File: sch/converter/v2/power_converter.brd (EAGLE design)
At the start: 54.6 x 28.2 mm, 23 parts

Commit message: Carrier board
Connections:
- new net SCL: U$1.P$29, U$1.P$30
- new net SDA: U$1.P$27, U$1.P$28
- net EXTVCC: no longer U$1.P$27, U$1.P$28, U$1.P$29, U$1.P$30
- net INTVCC: no longer U$1.P$23, U$1.P$24, U$1.P$25, U$1.P$26
- net PGOOD: now also U$1.P$25, U$1.P$26; no longer U$1.P$21, U$1.P$22
- net RUN: now also U$1.P$23, U$1.P$24; no longer U$1.P$19, U$1.P$20
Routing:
- net INTVCC: track 35.9 -> 0.00 mm, vias 3 -> 0
- net EXTVCC: track 31.0 -> 0.00 mm, vias 2 -> 0
- net SDA: track 0.00 -> 4.67 mm, vias 0 -> 1
- net SCL: track 0.00 -> 4.67 mm, vias 0 -> 1
- net PGOOD: track 12.5 -> 15.1 mm
- net RUN: track 18.7 -> 20.8 mm
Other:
- board text added: "ALAIN L. 10/2018"
- board text added: "REV: 2.1"
- board text added: "VIN: 4.5 to 36V"
- board text added: "VOUT: 0.8 to 24V"
- board text removed: "0.8 to 24V"
- board text removed: "4.5 to 36V"
- board text removed: "ALAIN L. 09/2018"
- board text removed: "REV: 2.0"

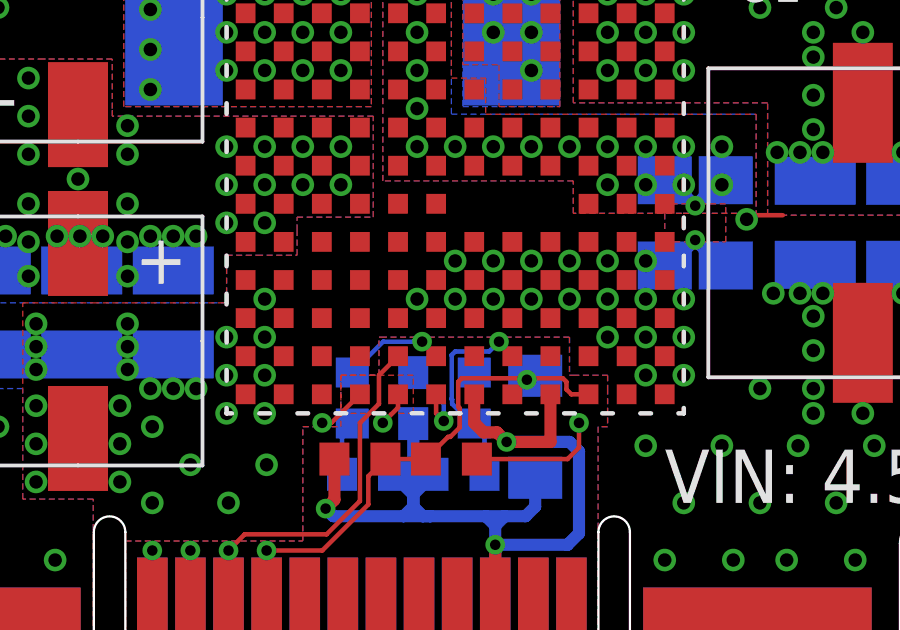
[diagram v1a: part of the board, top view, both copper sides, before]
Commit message: Added carrier BOM; Chaned carrier MOSFETs
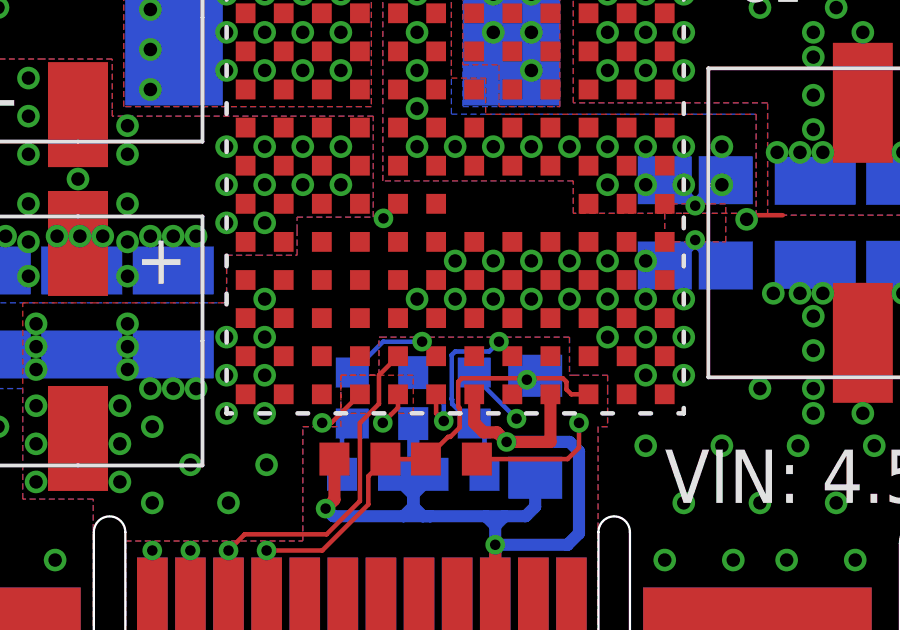
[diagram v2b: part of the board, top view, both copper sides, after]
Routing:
- net INTVCC: track 0.00 -> 18.4 mm, vias 0 -> 2
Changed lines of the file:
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@@
 <contactref element="U1" pad="F5"/>
 <contactref element="R6" pad="2"/>
-<wire x1="23.495" y1="27.2025" x2="20.955" y2="32.8295" width="0" layer="19" extent="1-16"/>
+<wire x1="20.955" y1="32.8295" x2="20.4696" y2="32.3441" width="0.1524" layer="1"/>
+<via x="20.4696" y="32.3441" extent="1-16" drill="0.35"/>
+<wire x1="20.4696" y1="32.3441" x2="20.4696" y2="31.5186" width="0.1524" layer="15"/>
+<wire x1="17.896" y1="25.7467875" x2="17.896" y2="25.3072125" width="0.1524" layer="15"/>
+<wire x1="18.7325" y1="26.5832875" x2="17.896" y2="25.7467875" width="0.1524" layer="15"/>
+<wire x1="17.896" y1="25.3072125" x2="18.2477125" y2="24.9555" width="0.1524" layer="15"/>
+<wire x1="18.7325" y1="29.7815" x2="18.7325" y2="26.5832875" width="0.1524" layer="15"/>
+<via x="24.90506875" y="25.66706875" extent="1-16" drill="0.35"/>
+<wire x1="24.3547125" y1="25.4226" x2="24.6606" y2="25.4226" width="0.1524" layer="15"/>
+<wire x1="24.6606" y1="25.4226" x2="24.90506875" y2="25.66706875" width="0.1524" layer="15"/>
+<wire x1="23.8876125" y1="24.9555" x2="24.3547125" y2="25.4226" width="0.1524" layer="15"/>
+<wire x1="18.2477125" y1="24.9555" x2="23.8876125" y2="24.9555" width="0.1524" layer="15"/>
+<wire x1="24.90506875" y1="25.66706875" x2="23.495" y2="27.0771375" width="0.1524" layer="16"/>
+<wire x1="23.495" y1="27.0771375" x2="23.495" y2="27.2025" width="0.1524" layer="16"/>
+<wire x1="20.4696" y1="31.5186" x2="18.7325" y2="29.7815" width="0.1524" layer="15"/>
 </signal>
 <signal name="PGOOD">

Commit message: Updated CAM files
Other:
- board text added: "NOTES: 1. Solder board in the folowing order: 1.1 Reflow solder top side using leaded solder paste with stencil 1.2 Hand solder bottom side 2. Solid silk-screen square to be used for noting designed output voltage 3. Card-edge style board fits into TE Connectivity Mini Crown Edge Connector P3S12 1926155-2"
- board text added: "REV: 2.0"
- board text removed: "Card-edge style board fits into TE Connectivity Mini Crown Edge Connector P3S12 1926155-2"
- board text removed: "REV: 2.1"
- board text removed: "Solid silk-screen square to be used for noting designed output voltage"
- board text removed: "Stencil and reflow soldering are required for board assembly"
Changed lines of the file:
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@@
 <?xml version="1.0" encoding="utf-8"?>
 <!DOCTYPE eagle SYSTEM "eagle.dtd">
-<eagle version="9.1.3">
+<eagle version="9.2.1">
 <drawing>
 <settings>
@@
 <grid distance="50" unitdist="mil" unit="mil" style="dots" multiple="1" display="yes" altdistance="2.5" altunitdist="mil" altunit="mil"/>
 <layers>
-<layer number="1" name="Top" color="4" fill="1" visible="yes" active="yes"/>
-<layer number="2" name="Route2" color="1" fill="3" visible="yes" active="yes"/>
+<layer number="1" name="Top" color="4" fill="1" visible="no" active="yes"/>
+<layer number="2" name="Route2" color="1" fill="3" visible="no" active="yes"/>
 <layer number="3" name="Route3" color="4" fill="3" visible="no" active="no"/>
 <layer number="4" name="Route4" color="1" fill="4" visible="no" active="no"/>
@@
 <layer number="13" name="Route13" color="4" fill="5" visible="no" active="no"/>
 <layer number="14" name="Route14" color="1" fill="6" visible="no" active="no"/>
-<layer number="15" name="Route15" color="4" fill="6" visible="yes" active="yes"/>
-<layer number="16" name="Bottom" color="1" fill="1" visible="yes" active="yes"/>
+<layer number="15" name="Route15" color="4" fill="6" visible="no" active="yes"/>
+<layer number="16" name="Bottom" color="1" fill="1" visible="no" active="yes"/>
 <layer number="17" name="Pads" color="2" fill="1" visible="yes" active="yes"/>
 <layer number="18" name="Vias" color="2" fill="1" visible="yes" active="yes"/>
-<layer number="19" name="Unrouted" color="6" fill="1" visible="yes" active="yes"/>
+<layer number="19" name="Unrouted" color="6" fill="1" visible="no" active="yes"/>
 <layer number="20" name="Dimension" color="24" fill="1" visible="yes" active="yes"/>
 <layer number="21" name="tPlace" color="7" fill="1" visible="yes" active="yes"/>
-<layer number="22" name="bPlace" color="7" fill="1" visible="yes" active="yes"/>
-<layer number="23" name="tOrigins" color="15" fill="1" visible="yes" active="yes"/>
-<layer number="24" name="bOrigins" color="15" fill="1" visible="yes" active="yes"/>
+<layer number="22" name="bPlace" color="7" fill="1" visible="no" active="yes"/>
+<layer number="23" name="tOrigins" color="15" fill="1" visible="no" active="yes"/>
+<layer number="24" name="bOrigins" color="15" fill="1" visible="no" active="yes"/>
 <layer number="25" name="tNames" color="7" fill="1" visible="yes" active="yes"/>
-<layer number="26" name="bNames" color="7" fill="1" visible="yes" active="yes"/>
+<layer number="26" name="bNames" color="7" fill="1" visible="no" active="yes"/>
 <layer number="27" name="tValues" color="7" fill="1" visible="no" active="yes"/>
 <layer number="28" name="bValues" color="7" fill="1" visible="no" active="yes"/>
 <layer number="29" name="tStop" color="7" fill="3" visible="yes" active="yes"/>
-<layer number="30" name="bStop" color="7" fill="6" visible="yes" active="yes"/>
+<layer number="30" name="bStop" color="7" fill="6" visible="no" active="yes"/>
 <layer number="31" name="tCream" color="7" fill="4" visible="yes" active="yes"/>
-<layer number="32" name="bCream" color="7" fill="5" visible="yes" active="yes"/>
-<layer number="33" name="tFinish" color="6" fill="3" visible="no" active="yes"/>
+<layer number="32" name="bCream" color="7" fill="5" visible="no" active="yes"/>
+<layer number="33" name="tFinish" color="6" fill="3" visible="yes" active="yes"/>
 <layer number="34" name="bFinish" color="6" fill="6" visible="no" active="yes"/>
 <layer number="35" name="tGlue" color="7" fill="4" visible="no" active="yes"/>
@@
 <layer number="37" name="tTest" color="7" fill="1" visible="no" active="yes"/>
 <layer number="38" name="bTest" color="7" fill="1" visible="no" active="yes"/>
-<layer number="39" name="tKeepout" color="4" fill="11" visible="yes" active="yes"/>
-<layer number="40" name="bKeepout" color="1" fill="11" visible="yes" active="yes"/>
-<layer number="41" name="tRestrict" color="4" fill="10" visible="yes" active="yes"/>
-<layer number="42" name="bRestrict" color="1" fill="10" visible="yes" active="yes"/>
+<layer number="39" name="tKeepout" color="4" fill="11" visible="no" active="yes"/>
+<layer number="40" name="bKeepout" color="1" fill="11" visible="no" active="yes"/>
+<layer number="41" name="tRestrict" color="4" fill="10" visible="no" active="yes"/>
+<layer number="42" name="bRestrict" color="1" fill="10" visible="no" active="yes"/>
 <layer number="43" name="vRestrict" color="2" fill="10" visible="no" active="yes"/>
 <layer number="44" name="Drills" color="7" fill="1" visible="no" active="yes"/>
 <layer number="45" name="Holes" color="7" fill="1" visible="no" active="yes"/>
-<layer number="46" name="Milling" color="3" fill="1" visible="yes" active="yes"/>
+<layer number="46" name="Milling" color="3" fill="1" visible="no" active="yes"/>
 <layer number="47" name="Measures" color="7" fill="1" visible="yes" active="yes"/>
 <layer number="48" name="Document" color="7" fill="1" visible="yes" active="yes"/>
@@
 <text x="40.7035" y="41.9735" size="1.27" layer="22" rot="MR180" align="bottom-right">MAX: 5A(Boost)
 10A(Buck)</text>
-<text x="83.82" y="10.16" size="1.778" layer="49">Stencil and reflow soldering
-are required for board assembly</text>
-<text x="83.82" y="0" size="1.778" layer="49">Solid silk-screen square to be used
-for noting designed output voltage</text>
-<text x="83.82" y="-13.97" size="1.778" layer="49">Card-edge style board fits into
-TE Connectivity Mini Crown Edge
-Connector P3S12 1926155-2</text>
+<text x="-96.52" y="-53.34" size="1.778" layer="49">NOTES:
+1. Solder board in the folowing order:
+  1.1 Reflow solder top side using leaded solder paste with stencil
+  1.2 Hand solder bottom side
+2. Solid silk-screen square to be used for noting designed output voltage
+3. Card-edge style board fits into TE Connectivity Mini Crown Edge Connector P3S12 1926155-2</text>
 <text x="2.54" y="43.1165" size="1.27" layer="21" align="top-center">REV:
-2.1</text>
+2.0</text>
 <dimension x1="62.23" y1="16.51" x2="62.23" y2="44.45" x3="71.12" y3="30.48" textsize="1.778" layer="48" visible="yes"/>
 <rectangle x1="43.18" y1="34.29" x2="50.8" y2="41.91" layer="25"/>
@@
 <attribute name="VALUE" x="19.05" y="22.4155" size="1.27" layer="27"/>
 </element>
-<element name="U$5" library="frames" library_urn="urn:adsk.eagle:library:229" package="A4L-LOC" value="" x="-104.14" y="-60.96"/>
-<element name="C7" library="LTM4607" package="PCR1H181MCL1GS" value="180u" x="36.449" y="32.1945"/>
+<element name="U$5" library="frames" library_urn="urn:adsk.eagle:library:229" package="A4L-LOC" value="" x="-104.14" y="-60.96" smashed="yes">
+<attribute name="DRAWING_NAME" x="113.03" y="-45.72" size="2.54" layer="48" font="vector"/>
+<attribute name="LAST_DATE_TIME" x="113.03" y="-50.8" size="2.286" layer="48" font="vector"/>
+</element>
+<element name="C7" library="LTM4607" package="PCR1H181MCL1GS" value="180u" x="36.449" y="32.1945" smashed="yes"/>
 <element name="R8" library="rcl" library_urn="urn:adsk.eagle:library:334" package="R0603" package3d_urn="urn:adsk.eagle:package:23555/2" value="6.98k" x="19.939" y="23.8125" smashed="yes" rot="MR0">
 <attribute name="SPICEPREFIX" value="R" x="19.939" y="23.8125" size="1.778" layer="28" rot="MR0" display="off"/>
@@
 </element>
 <element name="C14" library="LTM4607" package="PCR1V221MCL1GS" value="220u" x="10.287" y="39.0525" smashed="yes" rot="R180"/>
-<element name="U$1" library="LTM4607" package="1926155-2_CARD" value="1926155-2_CARD" x="25.4" y="16.51"/>
+<element name="U$1" library="LTM4607" package="1926155-2_CARD" value="1926155-2_CARD" x="25.4" y="16.51" smashed="yes"/>
 <element name="C2" library="rcl" library_urn="urn:adsk.eagle:library:334" package="C1210" package3d_urn="urn:adsk.eagle:package:23619/2" value="10u" x="7.366" y="29.21" smashed="yes" rot="MR270">
 <attribute name="SPICEPREFIX" value="C" x="7.366" y="29.21" size="1.778" layer="28" rot="MR270" display="off"/>

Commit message: Carrier rev. 1.4
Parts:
- added U$2: (no value), oshw:OSHW_8MM
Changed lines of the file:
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@@
 <?xml version="1.0" encoding="utf-8"?>
 <!DOCTYPE eagle SYSTEM "eagle.dtd">
-<eagle version="9.2.1">
+<eagle version="9.4.2">
 <drawing>
 <settings>
@@
 <grid distance="50" unitdist="mil" unit="mil" style="dots" multiple="1" display="yes" altdistance="2.5" altunitdist="mil" altunit="mil"/>
 <layers>
-<layer number="1" name="Top" color="4" fill="1" visible="no" active="yes"/>
-<layer number="2" name="Route2" color="1" fill="3" visible="no" active="yes"/>
+<layer number="1" name="Top" color="4" fill="1" visible="yes" active="yes"/>
+<layer number="2" name="Route2" color="1" fill="3" visible="yes" active="yes"/>
 <layer number="3" name="Route3" color="4" fill="3" visible="no" active="no"/>
 <layer number="4" name="Route4" color="1" fill="4" visible="no" active="no"/>
@@
 <layer number="13" name="Route13" color="4" fill="5" visible="no" active="no"/>
 <layer number="14" name="Route14" color="1" fill="6" visible="no" active="no"/>
-<layer number="15" name="Route15" color="4" fill="6" visible="no" active="yes"/>
-<layer number="16" name="Bottom" color="1" fill="1" visible="no" active="yes"/>
+<layer number="15" name="Route15" color="4" fill="6" visible="yes" active="yes"/>
+<layer number="16" name="Bottom" color="1" fill="1" visible="yes" active="yes"/>
 <layer number="17" name="Pads" color="2" fill="1" visible="yes" active="yes"/>
 <layer number="18" name="Vias" color="2" fill="1" visible="yes" active="yes"/>
-<layer number="19" name="Unrouted" color="6" fill="1" visible="no" active="yes"/>
+<layer number="19" name="Unrouted" color="6" fill="1" visible="yes" active="yes"/>
 <layer number="20" name="Dimension" color="24" fill="1" visible="yes" active="yes"/>
 <layer number="21" name="tPlace" color="7" fill="1" visible="yes" active="yes"/>
-<layer number="22" name="bPlace" color="7" fill="1" visible="no" active="yes"/>
-<layer number="23" name="tOrigins" color="15" fill="1" visible="no" active="yes"/>
-<layer number="24" name="bOrigins" color="15" fill="1" visible="no" active="yes"/>
+<layer number="22" name="bPlace" color="7" fill="1" visible="yes" active="yes"/>
+<layer number="23" name="tOrigins" color="15" fill="1" visible="yes" active="yes"/>
+<layer number="24" name="bOrigins" color="15" fill="1" visible="yes" active="yes"/>
 <layer number="25" name="tNames" color="7" fill="1" visible="yes" active="yes"/>
-<layer number="26" name="bNames" color="7" fill="1" visible="no" active="yes"/>
+<layer number="26" name="bNames" color="7" fill="1" visible="yes" active="yes"/>
 <layer number="27" name="tValues" color="7" fill="1" visible="no" active="yes"/>
 <layer number="28" name="bValues" color="7" fill="1" visible="no" active="yes"/>
-<layer number="29" name="tStop" color="7" fill="3" visible="yes" active="yes"/>
-<layer number="30" name="bStop" color="7" fill="6" visible="no" active="yes"/>
+<layer number="29" name="tStop" color="7" fill="3" visible="no" active="yes"/>
+<layer number="30" name="bStop" color="7" fill="6" visible="yes" active="yes"/>
 <layer number="31" name="tCream" color="7" fill="4" visible="yes" active="yes"/>
-<layer number="32" name="bCream" color="7" fill="5" visible="no" active="yes"/>
+<layer number="32" name="bCream" color="7" fill="5" visible="yes" active="yes"/>
 <layer number="33" name="tFinish" color="6" fill="3" visible="yes" active="yes"/>
 <layer number="34" name="bFinish" color="6" fill="6" visible="no" active="yes"/>
@@
 <layer number="43" name="vRestrict" color="2" fill="10" visible="no" active="yes"/>
 <layer number="44" name="Drills" color="7" fill="1" visible="no" active="yes"/>
-<layer number="45" name="Holes" color="7" fill="1" visible="no" active="yes"/>
-<layer number="46" name="Milling" color="3" fill="1" visible="no" active="yes"/>
+<layer number="45" name="Holes" color="7" fill="1" visible="yes" active="yes"/>
+<layer number="46" name="Milling" color="3" fill="1" visible="yes" active="yes"/>
 <layer number="47" name="Measures" color="7" fill="1" visible="yes" active="yes"/>
 <layer number="48" name="Document" color="7" fill="1" visible="yes" active="yes"/>
@@
 <attribute name="VALUE" x="41.91" y="27.94" size="1.27" layer="27" rot="R270"/>
 </element>
+<element name="U$2" library="oshw" package="OSHW_8MM" value="" x="5.08" y="39.37" smashed="yes" rot="MR0"/>
 </elements>
 <signals>
